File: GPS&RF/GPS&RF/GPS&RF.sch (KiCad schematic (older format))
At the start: 1 part, among them J2 Conn_01x09_Male

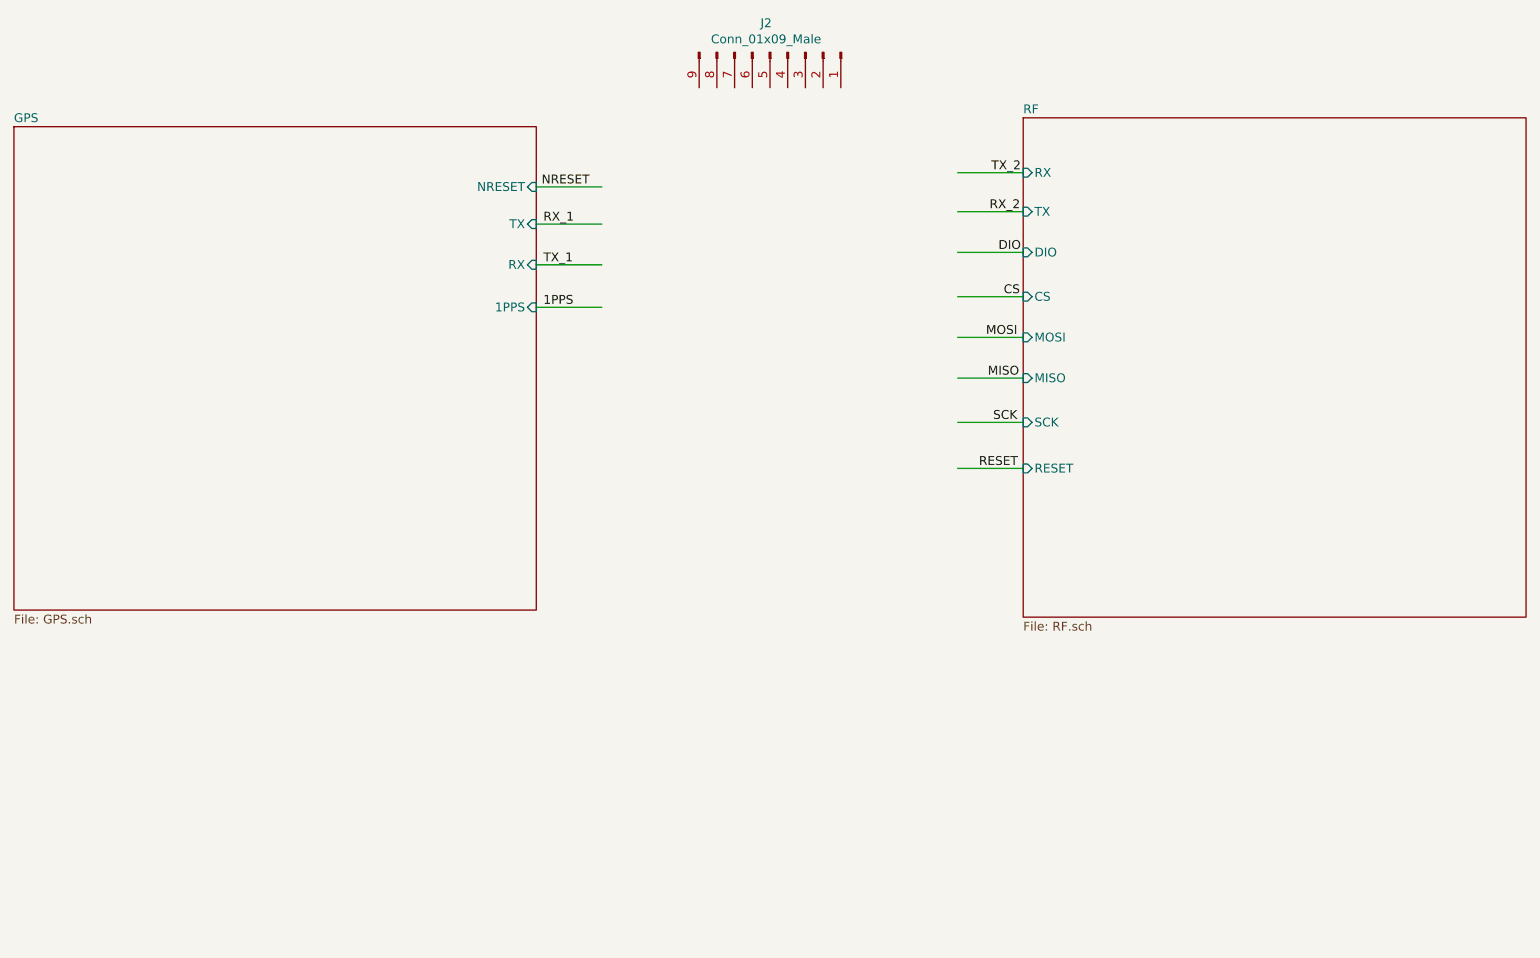
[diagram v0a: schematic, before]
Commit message: Finished the GPS&RF schematic
Replaced the 8 pin conn with a 13 pin conn_molex_PicoBlade
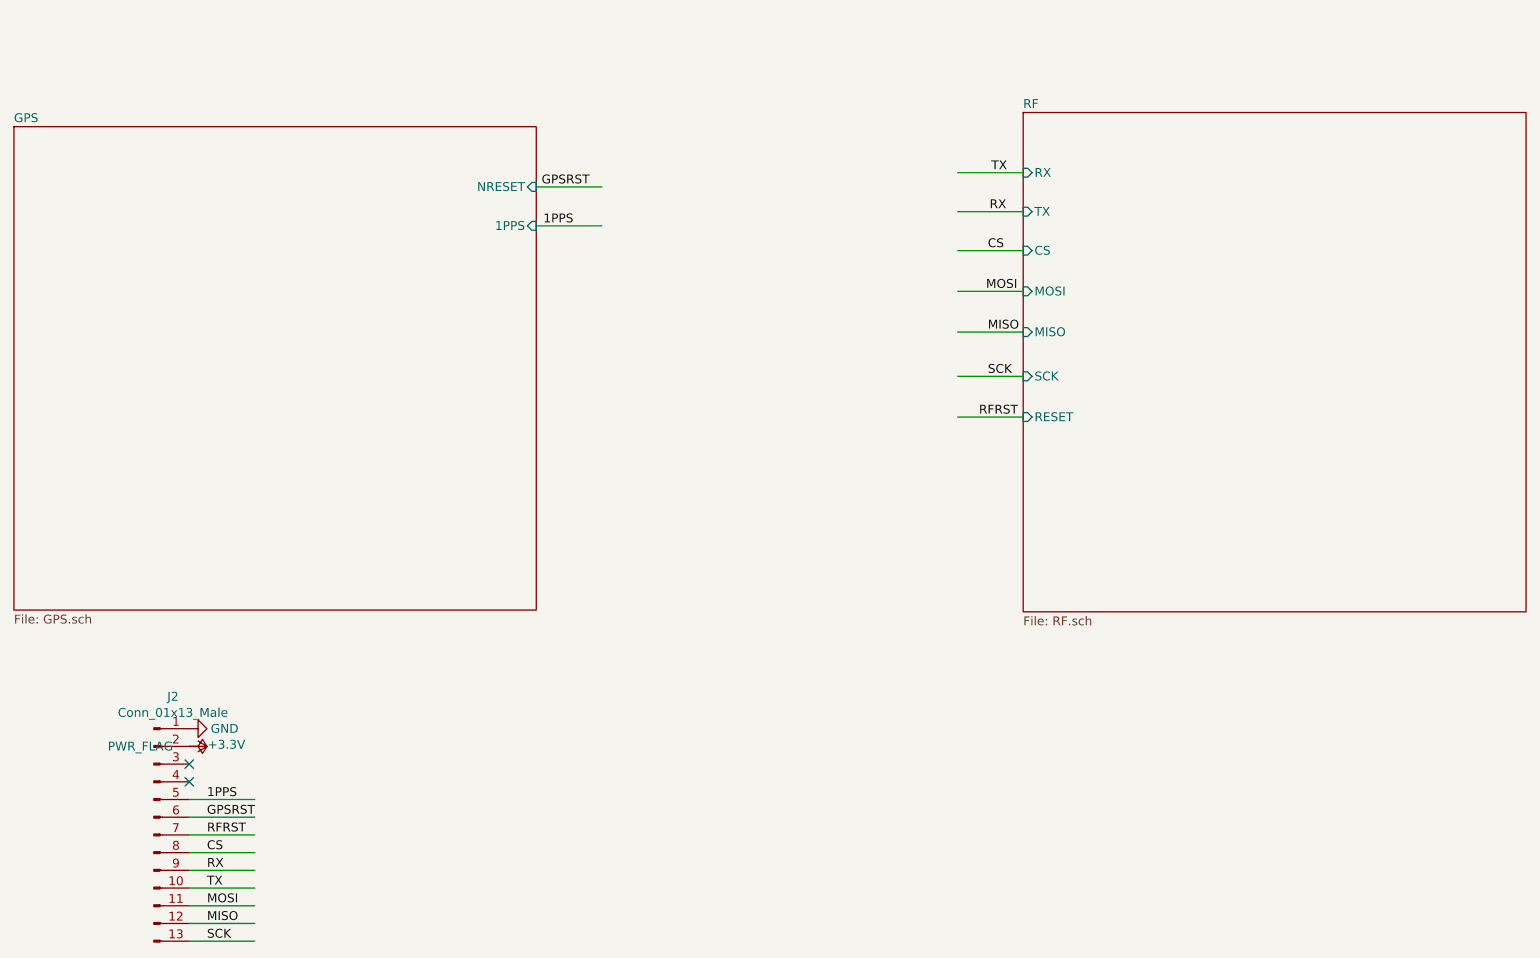
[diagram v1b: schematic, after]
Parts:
- removed J2: Conn_01x09_Male, Connector_Molex:Molex_PicoBlade_53048-0910_1x09_P1.25mm_Horizontal, symbol Connector:Conn_01x09_Male
- added J2: Conn_01x13_Male, Connector_Molex:Molex_PicoBlade_53048-1310_1x13_P1.25mm_Horizontal, symbol Connector:Conn_01x13_Male
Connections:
- net labels added: +3.3V, GND, GPSRST, RFRST, RX, TX
- net labels removed: DIO, NRESET, RESET, RX_1, RX_2, TX_1, TX_2
- wire segments 12 -> 18
- no-connect marks 0 -> 2
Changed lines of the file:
@@
 F1 "GPS.sch" 50
 F2 "NRESET" I R 4610 3070 50
-F3 "TX" I R 4610 3280 50
-F4 "RX" I R 4610 3510 50
-F5 "1PPS" I R 4610 3750 50
+F3 "1PPS" I R 4610 3290 50
 $EndSheet
 $Sheet
-S 7360 2680 2840 2820
+S 7360 2650 2840 2820
 U 60625EDB
 F0 "RF" 50
@@
 F2 "RX" I L 7360 2990 50
 F3 "TX" I L 7360 3210 50
-F4 "DIO" I L 7360 3440 50
-F5 "CS" I L 7360 3690 50
-F6 "MOSI" I L 7360 3920 50
-F7 "MISO" I L 7360 4150 50
-F8 "SCK" I L 7360 4400 50
-F9 "RESET" I L 7360 4660 50
+F4 "CS" I L 7360 3430 50
+F5 "MOSI" I L 7360 3660 50
+F6 "MISO" I L 7360 3890 50
+F7 "SCK" I L 7360 4140 50
+F8 "RESET" I L 7360 4370 50
 $EndSheet
 Wire Wire Line
 	4610 3070 4980 3070
 Wire Wire Line
-	4610 3280 4980 3280
-Wire Wire Line
-	4610 3510 4980 3510
-Wire Wire Line
-	4610 3750 4980 3750
+	4610 3290 4980 3290
 Wire Wire Line
 	6990 2990 7360 2990
@@
 	6990 3210 7360 3210
 Wire Wire Line
-	6990 3440 7360 3440
+	6990 3430 7360 3430
 Wire Wire Line
-	6990 3690 7360 3690
+	6990 3660 7360 3660
 Wire Wire Line
-	6990 3920 7360 3920
+	6990 3890 7360 3890
 Wire Wire Line
-	6990 4150 7360 4150
+	6990 4140 7360 4140
 Wire Wire Line
-	6990 4400 7360 4400
-Wire Wire Line
-	6990 4660 7360 4660
+	6990 4370 7360 4370
 Text Label 7180 2990 0    50   ~ 0
-TX_2
+TX
 Text Label 7170 3210 0    50   ~ 0
-RX_2
-Text Label 7220 3440 0    50   ~ 0
-DIO
-Text Label 7250 3690 0    50   ~ 0
+RX
+Text Label 7160 3430 0    50   ~ 0
 CS
-Text Label 7150 3920 0    50   ~ 0
+Text Label 7150 3660 0    50   ~ 0
 MOSI
-Text Label 7160 4150 0    50   ~ 0
+Text Label 7160 3890 0    50   ~ 0
 MISO
-Text Label 7190 4400 0    50   ~ 0
+Text Label 7160 4140 0    50   ~ 0
 SCK
-Text Label 7110 4660 0    50   ~ 0
-RESET
+Text Label 7110 4370 0    50   ~ 0
+RFRST
 Text Label 4640 3070 0    50   ~ 0
-NRESET
-Text Label 4650 3510 0    50   ~ 0
-TX_1
-Text Label 4650 3280 0    50   ~ 0
-RX_1
-Text Label 4650 3750 0    50   ~ 0
+GPSRST
+Text Label 4650 3290 0    50   ~ 0
 1PPS
 $Comp
-L Connector:Conn_01x09_Male J2
-U 1 1 6065EB87
-P 5930 2310
-F 0 "J2" V 5765 2288 50  0000 C CNN
-F 1 "Conn_01x09_Male" V 5856 2288 50  0000 C CNN
-F 2 "Connector_Molex:Molex_PicoBlade_53048-0910_1x09_P1.25mm_Horizontal" H 5930 2310 50  0001 C CNN
-F 3 "https://www.molex.com/webdocs/datasheets/pdf/en-us/0530480910_PCB_HEADERS.pdf" H 5930 2310 50  0001 C CNN
-F 4 "https://www.digikey.com/en/products/detail/molex/0530480910/242871?WT.z_cid=sp_900_0310_buynow&s=N4IgTCBcDaIAwFYDMcAsAOOBOAjHEAugL5A" V 5930 2310 50  0001 C CNN "Order Link"
-	1    5930 2310
+L Connector:Conn_01x13_Male J2
+U 1 1 61217AA0
+P 2450 6730
+F 0 "J2" H 2558 7511 50  0000 C CNN
+F 1 "Conn_01x13_Male" H 2558 7420 50  0000 C CNN
+F 2 "Connector_Molex:Molex_PicoBlade_53048-1310_1x13_P1.25mm_Horizontal" H 2450 6730 50  0001 C CNN
+F 3 "https://www.molex.com/webdocs/datasheets/pdf/en-us/0530481310_PCB_HEADERS.pdf" H 2450 6730 50  0001 C CNN
+	1    2450 6730
+	1    0    0    -1
+$EndComp
+$Comp
+L power:GND #PWR0113
+U 1 1 6121CE60
+P 2650 6130
+F 0 "#PWR0113" H 2650 5880 50  0001 C CNN
+F 1 "GND" V 2650 5930 50  0000 C CNN
+F 2 "" H 2650 6130 50  0001 C CNN
+F 3 "" H 2650 6130 50  0001 C CNN
+	1    2650 6130
+	0    -1   -1   0
+$EndComp
+$Comp
+L power:+3.3V #PWR0114
+U 1 1 6121D2C0
+P 2650 6230
+F 0 "#PWR0114" H 2650 6080 50  0001 C CNN
+F 1 "+3.3V" V 2640 6440 50  0000 C CNN
+F 2 "" H 2650 6230 50  0001 C CNN
+F 3 "" H 2650 6230 50  0001 C CNN
+	1    2650 6230
 	0    1    1    0
 $EndComp
+Wire Wire Line
+	3020 6530 2650 6530
+Wire Wire Line
+	3020 6630 2650 6630
+Wire Wire Line
+	3020 6730 2650 6730
+Wire Wire Line
+	3020 6830 2650 6830
+Wire Wire Line
+	3020 7130 2650 7130
+Wire Wire Line
+	3020 7230 2650 7230
+Wire Wire Line
+	3020 7330 2650 7330
+Text Label 2750 6530 0    50   ~ 0
+1PPS
+Text Label 2750 6630 0    50   ~ 0
+GPSRST
+Text Label 2750 6730 0    50   ~ 0
+RFRST
+Text Label 2750 6830 0    50   ~ 0
+CS
+Text Label 2750 7130 0    50   ~ 0
+MOSI
+Text Label 2750 7230 0    50   ~ 0
+MISO
+Text Label 2750 7330 0    50   ~ 0
+SCK
+Wire Wire Line
+	3020 6930 2650 6930
+Wire Wire Line
+	3020 7030 2650 7030
+Text Label 2750 6930 0    50   ~ 0
+RX
+Text Label 2750 7030 0    50   ~ 0
+TX
+NoConn ~ 2650 6330
+NoConn ~ 2650 6430
+$Comp
+L power:PWR_FLAG #FLG0102
+U 1 1 612340ED
+P 2650 6230
+F 0 "#FLG0102" H 2650 6305 50  0001 C CNN
+F 1 "PWR_FLAG" V 2650 5770 50  0000 L CNN
+F 2 "" H 2650 6230 50  0001 C CNN
+F 3 "~" H 2650 6230 50  0001 C CNN
+	1    2650 6230
+	0    1    1    0
+$EndComp

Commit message: Finished SCH and PCB
Finished everything, might need to edit a few things but pushing the 'final' now
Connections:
- net labels added: RX_D1, RX_D2, TX_D1, TX_D2
- net labels removed: RX, TX
- wire segments 18 -> 22
- no-connect marks 2 -> 0
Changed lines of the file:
@@
 F1 "GPS.sch" 50
 F2 "NRESET" I R 4610 3070 50
-F3 "1PPS" I R 4610 3290 50
+F3 "1PPS" I R 4610 3270 50
+F4 "TX_D2" I R 4610 3460 50
+F5 "RX_D2" I R 4610 3660 50
 $EndSheet
 $Sheet
@@
 F0 "RF" 50
 F1 "RF.sch" 50
-F2 "RX" I L 7360 2990 50
-F3 "TX" I L 7360 3210 50
+F2 "RX_D1" I L 7360 2990 50
+F3 "TX_D1" I L 7360 3210 50
 F4 "CS" I L 7360 3430 50
 F5 "MOSI" I L 7360 3660 50
@@
 	4610 3070 4980 3070
 Wire Wire Line
-	4610 3290 4980 3290
+	4610 3270 4980 3270
 Wire Wire Line
 	6990 2990 7360 2990
@@
 Wire Wire Line
 	6990 4370 7360 4370
-Text Label 7180 2990 0    50   ~ 0
-TX
-Text Label 7170 3210 0    50   ~ 0
-RX
+Text Label 7130 2990 0    50   ~ 0
+TX_D1
+Text Label 7120 3210 0    50   ~ 0
+RX_D1
 Text Label 7160 3430 0    50   ~ 0
 CS
@@
 Text Label 4640 3070 0    50   ~ 0
 GPSRST
-Text Label 4650 3290 0    50   ~ 0
+Text Label 4650 3270 0    50   ~ 0
 1PPS
 $Comp
@@
 	3020 7030 2650 7030
 Text Label 2750 6930 0    50   ~ 0
-RX
+RX_D1
 Text Label 2750 7030 0    50   ~ 0
-TX
-NoConn ~ 2650 6330
-NoConn ~ 2650 6430
+TX_D1
 $Comp
 L power:PWR_FLAG #FLG0102
@@
 	0    1    1    0
 $EndComp
+Wire Wire Line
+	4610 3460 4980 3460
+Wire Wire Line
+	4610 3660 4980 3660
+Text Label 4650 3460 0    50   ~ 0
+RX_D2
+Text Label 4650 3660 0    50   ~ 0
+TX_D2
+Wire Wire Line
+	2650 6430 3020 6430
+Wire Wire Line
+	2650 6330 3020 6330
+Text Label 2760 6330 0    50   ~ 0
+RX_D2
+Text Label 2760 6430 0    50   ~ 0
+TX_D2
 $EndSCHEMATC
